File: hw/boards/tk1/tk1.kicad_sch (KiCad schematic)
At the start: 0 parts

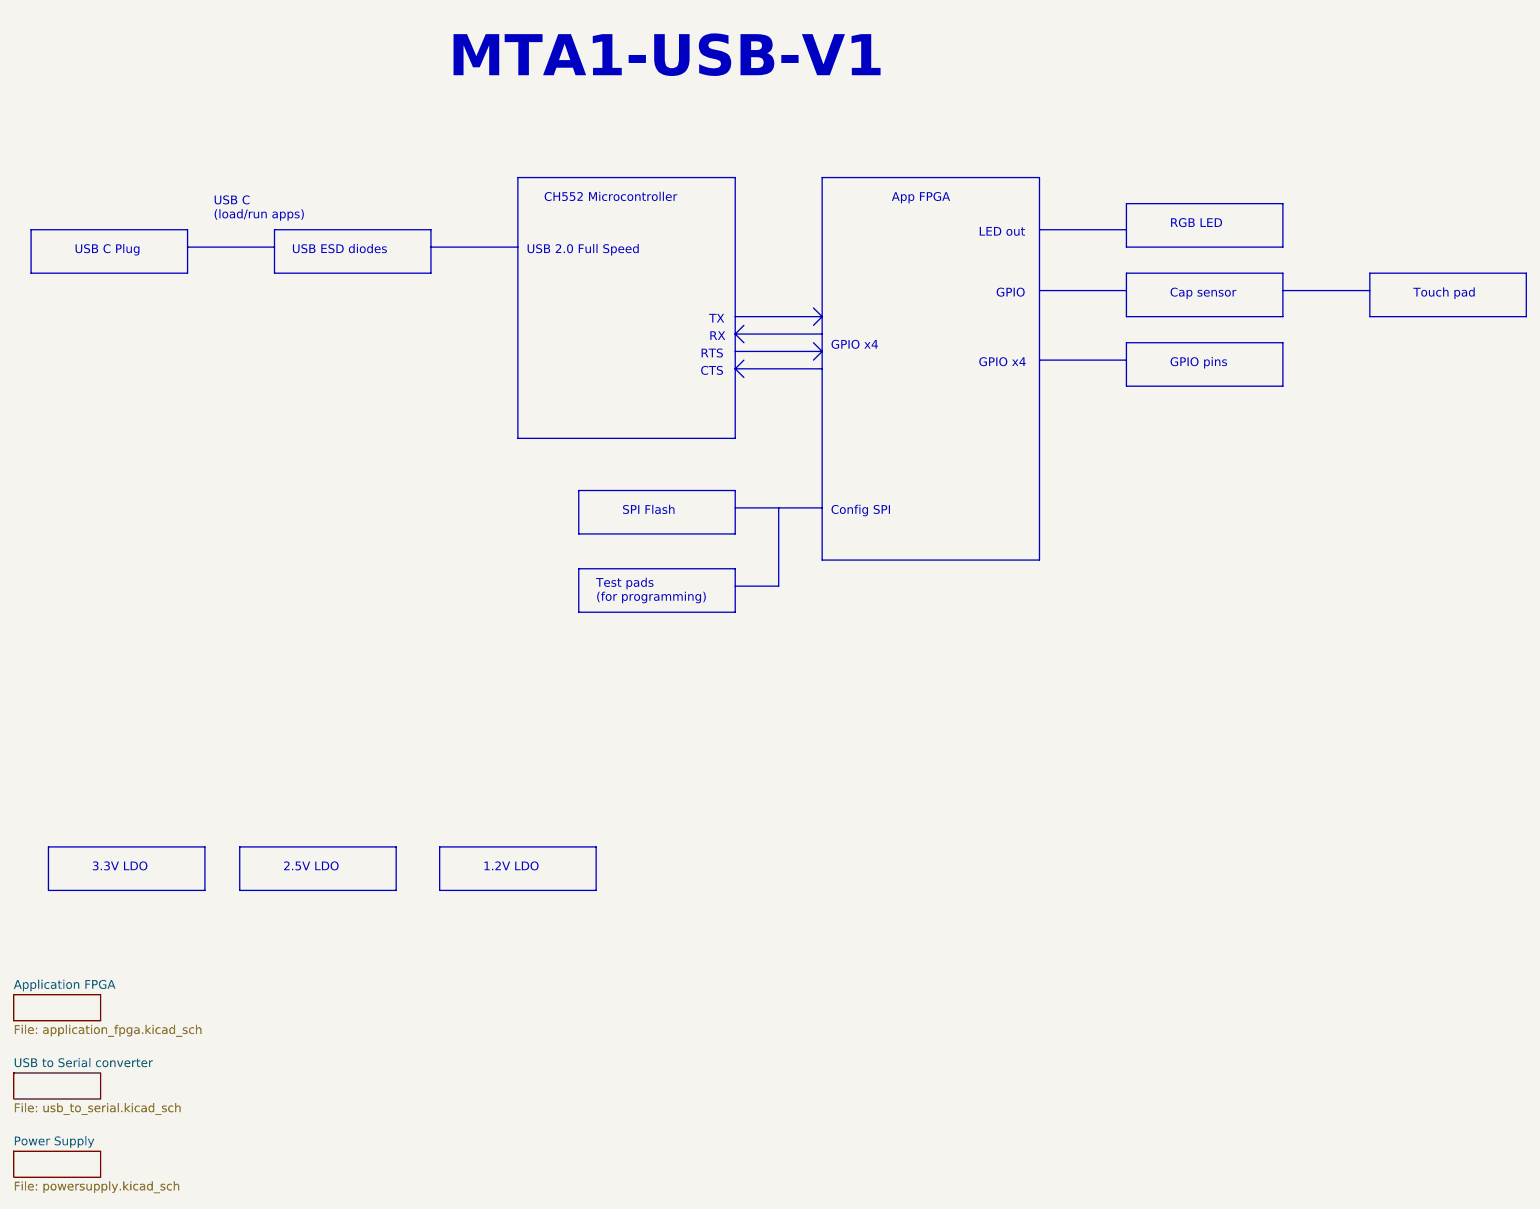
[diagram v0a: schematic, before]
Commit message: TK-1 and TP-1 PCBs (#52)
* Add kicad library for flat programming clip

* Add descriptions to part symbols

* Add extended values, manufacturer/distributor info to components in mta1

* Add new board entry for TK1

* Add TP1 programmer design

* Update MTA1-USB-V1 release files to match production

* Change SPI flash memory type to XT25F08BDFIGT-S
* Change touch sensor feedback cap to 1uF
* Add manufacturer, manufacturer part number, distributor, distributor part number

* Update component values for TK1 PCB

* Use specific part # for C8
* Change flash back to Winbond part, for easier sourcing
* Change C1 to 1pF

* Fixes for production programmer PCB

* Swap GND and 5V on J3
* Replace graphic logo with text
* Rename part to 'TP-1'

* TK-1 release

* Add dimensions for PCB
* Add layer stackup for PCB
* Change PCB component origin to match expanded board
* Change schematic title to 'TK-1', update release date

* mta1-usb-v1-programmer: Add corrected part numbers for OSFC production

* Q1, Q2, F1 part subsititutions
* add mfr/supplier info for all parts

* PCB library: add parts

* Rectangular footprint for TK-1 test pads
* BOM generation script used for TK-1 and TP-1 releases

* TP-1 release

* Schematic: Add manufacturer, supplier information for all parts
* Schematic: Update name and release date
* PCB: Add PCB fabrication information
* PCB: Correct pinouts on silkscreen

* PCB library: add 'screw' and 'foot' symbols

* Screw is a schematic-only part, for including mechanical screws in the
  BOM
* Foot is for self-adhesive rubber mounting feet that can be stuck to
  the bottom of a PCB

* TP-1 release: Add screws, feet to the BOM

* Pico library: Add footprint for RPi Pico w/solder paste

* TP-1 RevA release updates:

* Add fiducials in 3 corners (1mm exposed copper ring w/2mm soldermask opening)
* Add solder paste openings to Raspberry Pi Pico pads

* TK-1: RevA.1 release

* Add two fiducials to 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
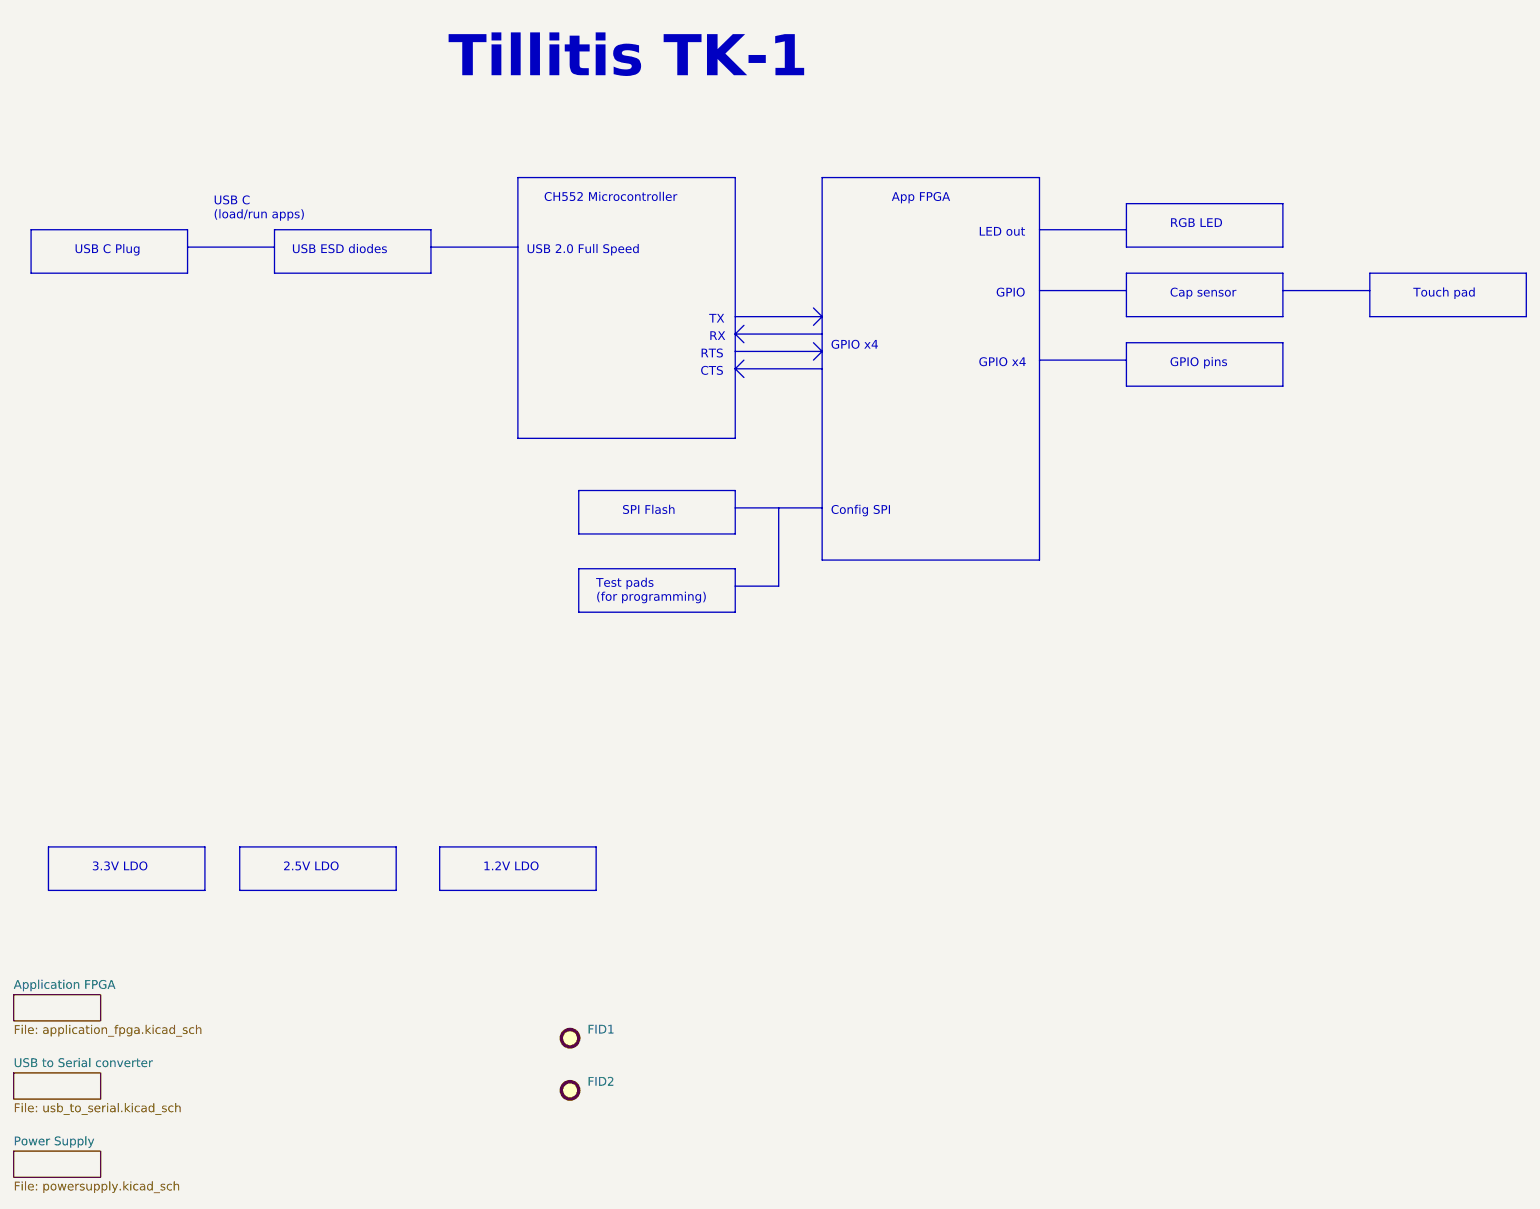
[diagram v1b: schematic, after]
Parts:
- added FID1, FID2: (no value), symbol Mechanical:Fiducial
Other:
- note added: "Tillitis TK-1"
- note removed: "MTA1-USB-V1"
- title: MTA1-USB-V1 -> TK-1
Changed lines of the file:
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@@
   (paper "A4")
   (title_block
-    (title "MTA1-USB-V1")
-    (date "2021-09-29")
+    (title "TK-1")
+    (date "2021-11-14")
     (rev "V1")
     (company "Tillitis AB")
@@
     (effects (font (size 1.27 1.27)) (justify left bottom))
   )
-  (text "MTA1-USB-V1" (at 106.68 24.13 0)
+  (text "Tillitis TK-1" (at 106.68 24.13 0)
     (effects (font (size 6 6) (thickness 0.254) bold) (justify left bottom))
   )
@@
   (text "Test pads\n(for programming)" (at 128.27 100.33 0)
     (effects (font (size 1.27 1.27)) (justify left bottom))
+  )
+  (symbol (lib_id "Mechanical:Fiducial") (at 124.46 163.83 90) (unit 1)
+    (in_bom no) (on_board yes) (fields_autoplaced)
+    (property "Reference" "FID1" (id 0) (at 127 162.5599 90)
+      (effects (font (size 1.27 1.27)) (justify right))
+    )
+    (property "Value" "" (id 1) (at 127 165.0999 90)
+      (effects (font (size 1.27 1.27)) (justify right))
+    )
+    (property "Footprint" "" (id 2) (at 124.46 163.83 0)
+      (effects (font (size 1.27 1.27)) hide)
+    )
+    (property "Datasheet" "~" (id 3) (at 124.46 163.83 0)
+      (effects (font (size 1.27 1.27)) hide)
+    )
+  )
+  (symbol (lib_id "Mechanical:Fiducial") (at 124.46 171.45 90) (unit 1)
+    (in_bom no) (on_board yes) (fields_autoplaced)
+    (property "Reference" "FID2" (id 0) (at 127 170.1799 90)
+      (effects (font (size 1.27 1.27)) (justify right))
+    )
+    (property "Value" "" (id 1) (at 127 172.7199 90)
+      (effects (font (size 1.27 1.27)) (justify right))
+    )
+    (property "Footprint" "" (id 2) (at 124.46 171.45 0)
+      (effects (font (size 1.27 1.27)) hide)
+    )
+    (property "Datasheet" "~" (id 3) (at 124.46 171.45 0)
+      (effects (font (size 1.27 1.27)) hide)
+    )
   )
   (sheet (at 43.18 180.34) (size 12.7 3.81) (fields_autoplaced)
@@
     )
     (path "/00000000-0000-0000-0000-0000611cc101/0f8bd06f-60b1-4be8-90d9-1a7f1cd60020"
-      (reference "C8") (unit 1) (value "10uF") (footprint "Capacitor_SMD:C_1206_3216Metric")
+      (reference "C8") (unit 1) (value "1uF") (footprint "Capacitor_SMD:C_1206_3216Metric")
     )
     (path "/00000000-0000-0000-0000-00006161400b/00000000-0000-0000-0000-0000617f1504"
@@
     )
     (path "/00000000-0000-0000-0000-0000611cc101/391c56db-bc39-4ec7-bb45-dcbe1aaf2b1a"
-      (reference "C27") (unit 1) (value "2.7pF") (footprint "mta1:CAPC1005X06L")
+      (reference "C27") (unit 1) (value "1pF") (footprint "mta1:CAPC1005X06L")
     )
     (path "/00000000-0000-0000-0000-0000611a4eb9/00000000-0000-0000-0000-0000618029cb"
@@
       (reference "FB3") (unit 1) (value "BLM18KG300TN1D") (footprint "mta1:Ferritbead_0603_1608Metric")
     )
+    (path "/59501395-780b-47e4-8967-9f965674a799"
+      (reference "FID1") (unit 1) (value "Fiducial") (footprint "Fiducial:Fiducial_0.75mm_Mask1.5mm")
+    )
+    (path "/bf741fd1-5855-4a31-8c21-db9bc5f783af"
+      (reference "FID2") (unit 1) (value "Fiducial") (footprint "Fiducial:Fiducial_0.75mm_Mask1.5mm")
+    )
     (path "/00000000-0000-0000-0000-00006161400b/7b422c5e-fd7b-4ac9-8400-966a18c34fdc"
       (reference "P1") (unit 1) (value "USB_C_Plug") (footprint "mta1:U261-241N-4BS60")
@@
     )
     (path "/00000000-0000-0000-0000-0000611a4eb9/00000000-0000-0000-0000-000061804e06"
-      (reference "TP1") (unit 1) (value "5V") (footprint "TestPoint:TestPoint_Pad_D1.0mm")
+      (reference "TP1") (unit 1) (value "5V") (footprint "mta1:TestPoint_Pad_D1.0mm")
     )
     (path "/00000000-0000-0000-0000-0000611a4eb9/00000000-0000-0000-0000-000061290a70"
-      (reference "TP2") (unit 1) (value "3V3") (footprint "TestPoint:TestPoint_Pad_D1.0mm")
+      (reference "TP2") (unit 1) (value "3V3") (footprint "mta1:TestPoint_Pad_D1.0mm")
     )
     (path "/00000000-0000-0000-0000-0000611a4eb9/00000000-0000-0000-0000-000061293ed2"
-      (reference "TP3") (unit 1) (value "2V5") (footprint "TestPoint:TestPoint_Pad_D1.0mm")
+      (reference "TP3") (unit 1) (value "2V5") (footprint "mta1:TestPoint_Pad_D1.0mm")
     )
     (path "/00000000-0000-0000-0000-0000611a4eb9/00000000-0000-0000-0000-0000612c6885"
-      (reference "TP4") (unit 1) (value "1V2") (footprint "TestPoint:TestPoint_Pad_D1.0mm")
+      (reference "TP4") (unit 1) (value "1V2") (footprint "mta1:TestPoint_Pad_D1.0mm")
     )
     (path "/00000000-0000-0000-0000-0000611cc101/ab35f289-cbe7-449b-a15d-459a3b4e9240"
-      (reference "TP5") (unit 1) (value "APP_GND") (footprint "TestPoint:TestPoint_Pad_D1.0mm")
+      (reference "TP5") (unit 1) (value "APP_GND") (footprint "mta1:TestPoint_Pad_D1.0mm")
     )
     (path "/00000000-0000-0000-0000-00006161400b/fb64afad-a905-4f4b-98a2-d21a64bd12f3"
-      (reference "TP6") (unit 1) (value "INT_TX") (footprint "TestPoint:TestPoint_Pad_D1.0mm")
+      (reference "TP6") (unit 1) (value "INT_TX") (footprint "mta1:TestPoint_Pad_D1.0mm")
     )
     (path "/00000000-0000-0000-0000-00006161400b/1f54ffea-0a26-464d-98d4-30979db7344f"
-      (reference "TP7") (unit 1) (value "INT_RX") (footprint "TestPoint:TestPoint_Pad_D1.0mm")
+      (reference "TP7") (unit 1) (value "INT_RX") (footprint "mta1:TestPoint_Pad_D1.0mm")
     )
     (path "/00000000-0000-0000-0000-00006161400b/74f30866-0d52-4558-88d9-da85c982a4ac"
-      (reference "TP8") (unit 1) (value "INT_RTS") (footprint "TestPoint:TestPoint_Pad_D1.0mm")
+      (reference "TP8") (unit 1) (value "INT_RTS") (footprint "mta1:TestPoint_Pad_D1.0mm")
     )
     (path "/00000000-0000-0000-0000-00006161400b/d9fa1bba-ba87-4376-952a-41bb8392f957"
-      (reference "TP9") (unit 1) (value "INT_CTS") (footprint "TestPoint:TestPoint_Pad_D1.0mm")
+      (reference "TP9") (unit 1) (value "INT_CTS") (footprint "mta1:TestPoint_Pad_D1.0mm")
     )
     (path "/00000000-0000-0000-0000-0000611cc101/b84f4f68-cc10-43a0-962e-10a1890e7eaf"
-      (reference "TP12") (unit 1) (value "APP_ICE_SCK") (footprint "TestPoint:TestPoint_Pad_D1.0mm")
+      (reference "TP12") (unit 1) (value "APP_ICE_SCK") (footprint "mta1:TestPoint_Pad_D1.0mm")
     )
     (path "/00000000-0000-0000-0000-0000611cc101/f77c0061-34af-41f5-8a00-bb8ae07fe922"
-      (reference "TP13") (unit 1) (value "APP_ICE_SS") (footprint "TestPoint:TestPoint_Pad_D1.0mm")
+      (reference "TP13") (unit 1) (value "APP_ICE_SS") (footprint "mta1:TestPoint_Pad_D1.0mm")
     )
     (path "/00000000-0000-0000-0000-0000611cc101/3c9864fc-0a77-4fe0-8c96-c0260a516ba1"
-      (reference "TP14") (unit 1) (value "APP_ICE_MOSI") (footprint "TestPoint:TestPoint_Pad_D1.0mm")
+      (reference "TP14") (unit 1) (value "APP_ICE_MOSI") (footprint "mta1:TestPoint_Pad_D1.0mm")
     )
     (path "/00000000-0000-0000-0000-0000611cc101/0f9d611d-221f-42fe-a161-07c0ff52c542"
-      (reference "TP15") (unit 1) (value "APP_ICE_MISO") (footprint "TestPoint:TestPoint_Pad_D1.0mm")
+      (reference "TP15") (unit 1) (value "APP_ICE_MISO") (footprint "mta1:TestPoint_Pad_D1.0mm")
     )
     (path "/00000000-0000-0000-0000-0000611cc101/d7bf813c-bb4e-4ed8-b86f-d9ec1d86656d"
-      (reference "TP16") (unit 1) (value "APP_CRESET") (footprint "TestPoint:TestPoint_Pad_D1.0mm")
+      (reference "TP16") (unit 1) (value "APP_CRESET") (footprint "mta1:TestPoint_Pad_D1.0mm")
     )
     (path "/00000000-0000-0000-0000-0000611cc101/32f54cf3-1e0f-4aaa-b508-267b9568217c"
-      (reference "TP17") (unit 1) (value "APP_CDONE") (footprint "TestPoint:TestPoint_Pad_D1.0mm")
+      (reference "TP17") (unit 1) (value "APP_CDONE") (footprint "mta1:TestPoint_Pad_D1.0mm")
     )
     (path "/00000000-0000-0000-0000-0000611cc101/e7d44998-7d27-4371-9f3d-0a968eddee9d"
-      (reference "TP18") (unit 1) (value "APP_GPIO1") (footprint "TestPoint:TestPoint_Pad_D1.0mm")
+      (reference "TP18") (unit 1) (value "APP_GPIO1") (footprint "mta1:TestPoint_Pad_D1.0mm")
     )
     (path "/00000000-0000-0000-0000-0000611cc101/855a271d-d14e-4340-88ef-5eb1d2805d77"
-      (reference "TP19") (unit 1) (value "APP_GPIO2") (footprint "TestPoint:TestPoint_Pad_D1.0mm")
+      (reference "TP19") (unit 1) (value "APP_GPIO2") (footprint "mta1:TestPoint_Pad_D1.0mm")
     )
     (path "/00000000-0000-0000-0000-0000611cc101/8aa5c85f-46b3-4ac4-bd48-3e3352ebb3f6"
-      (reference "TP20") (unit 1) (value "APP_GPIO3") (footprint "TestPoint:TestPoint_Pad_D1.0mm")
+      (reference "TP20") (unit 1) (value "APP_GPIO3") (footprint "mta1:TestPoint_Pad_D1.0mm")
     )
     (path "/00000000-0000-0000-0000-0000611cc101/a6d52094-2dbe-49fa-99c1-8b125d3ae4c6"
-      (reference "TP21") (unit 1) (value "APP_GPIO4") (footprint "TestPoint:TestPoint_Pad_D1.0mm")
+      (reference "TP21") (unit 1) (value "APP_GPIO4") (footprint "mta1:TestPoint_Pad_D1.0mm")
     )
     (path "/00000000-0000-0000-0000-0000611a4eb9/f74c1147-0f6c-4852-95d4-43a254720c79"
-      (reference "TP28") (unit 1) (value "GND") (footprint "TestPoint:TestPoint_Pad_D1.0mm")
+      (reference "TP28") (unit 1) (value "GND") (footprint "mta1:TestPoint_Pad_D1.0mm")
     )
     (path "/00000000-0000-0000-0000-0000611a4eb9/00000000-0000-0000-0000-00006126a5e3"
@@
     )
     (path "/00000000-0000-0000-0000-0000611cc101/fb1bfba7-59bf-4387-b0fd-53ae34c08235"
-      (reference "U8") (unit 1) (value "XT25F08BDFIGT-S") (footprint "mta1:W25Q80DVUXIE")
+      (reference "U8") (unit 1) (value "W25Q80DVUXIE") (footprint "mta1:W25Q80DVUXIE")
     )
     (path "/00000000-0000-0000-0000-0000611a4eb9/00000000-0000-0000-0000-0000616b8c22"
